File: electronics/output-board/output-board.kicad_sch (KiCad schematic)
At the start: 45 parts, among them J14 Arming switch, J17 Conn_01x02_Male, J19 Extra IO, J20 Ignition Detector, J3 12V In, J4 Conn_01x02, J5 SWD Header, J6 Conn_01x02, SW1 SW_Push_Dual, U1 MAX33012EASA+, U2 LD3985M33R_SOT23, U3 STM32F105VBH6, Y1 36MHz 9pF

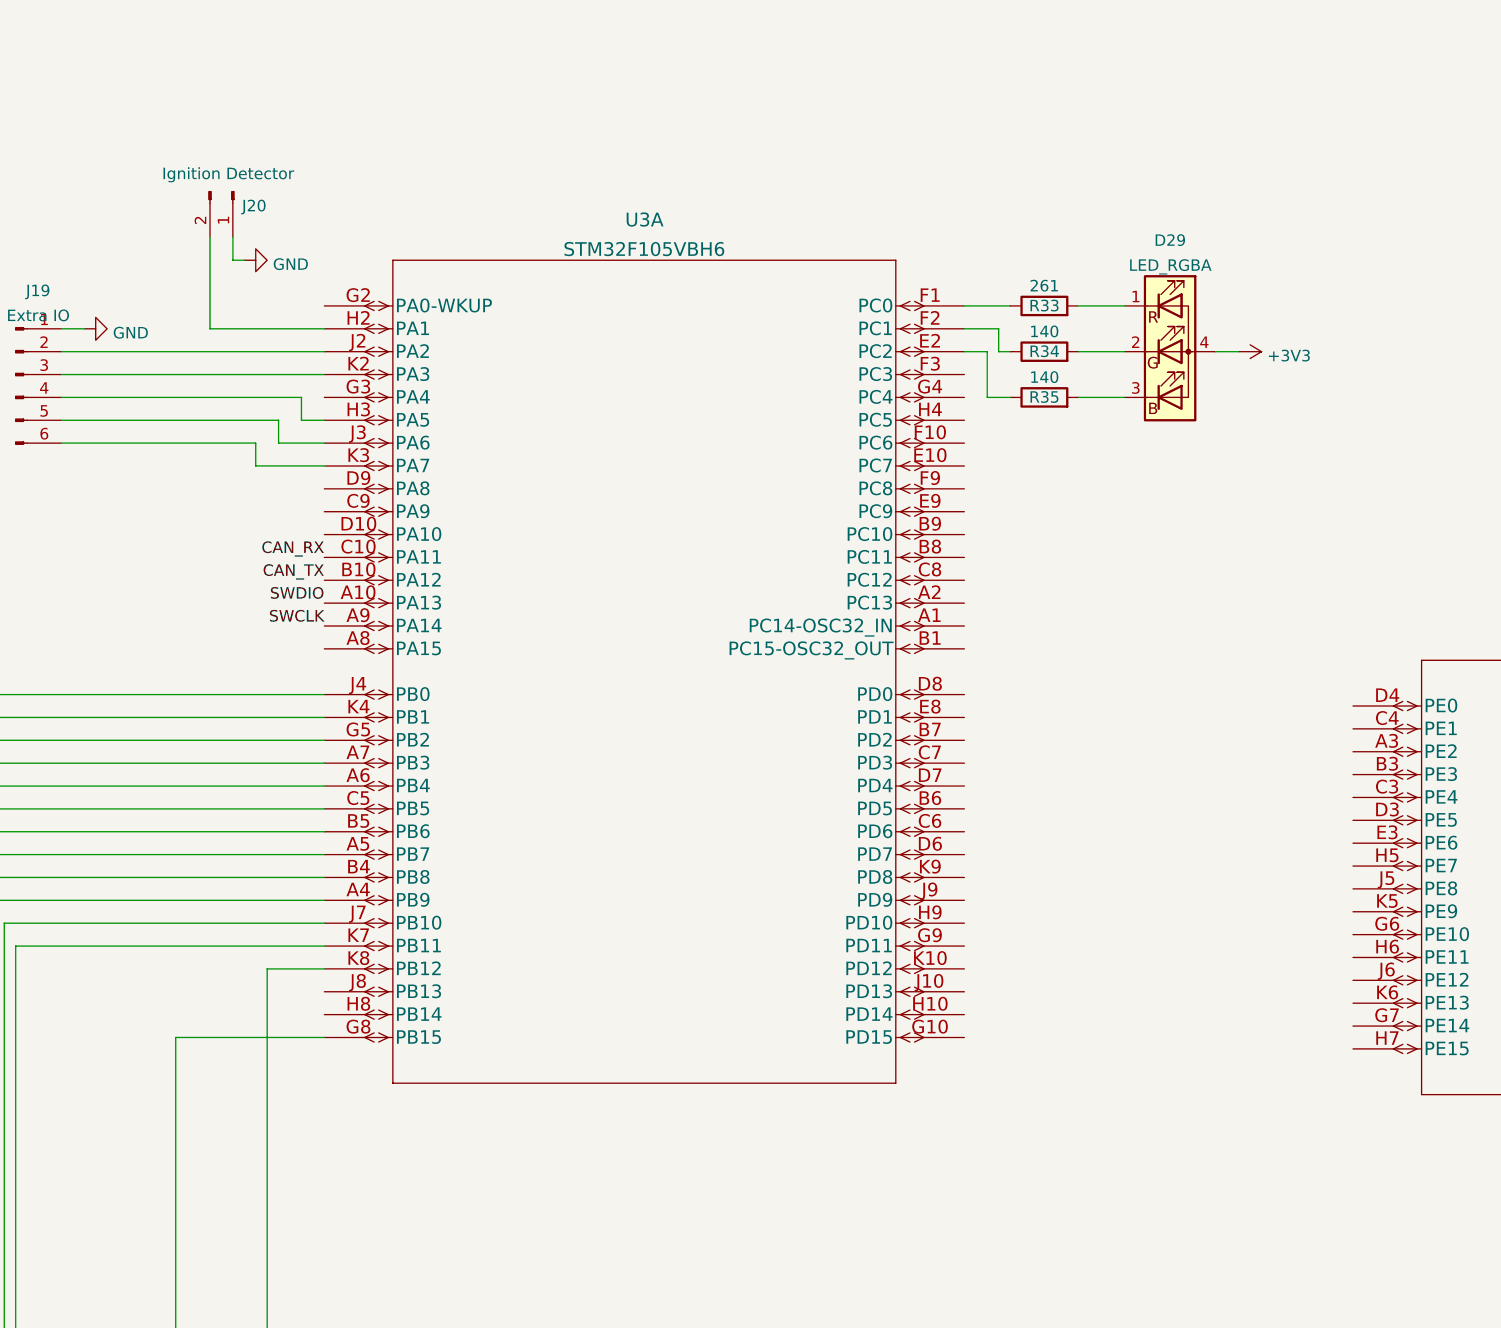
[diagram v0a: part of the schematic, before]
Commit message: Finishing touches on output board rev 2
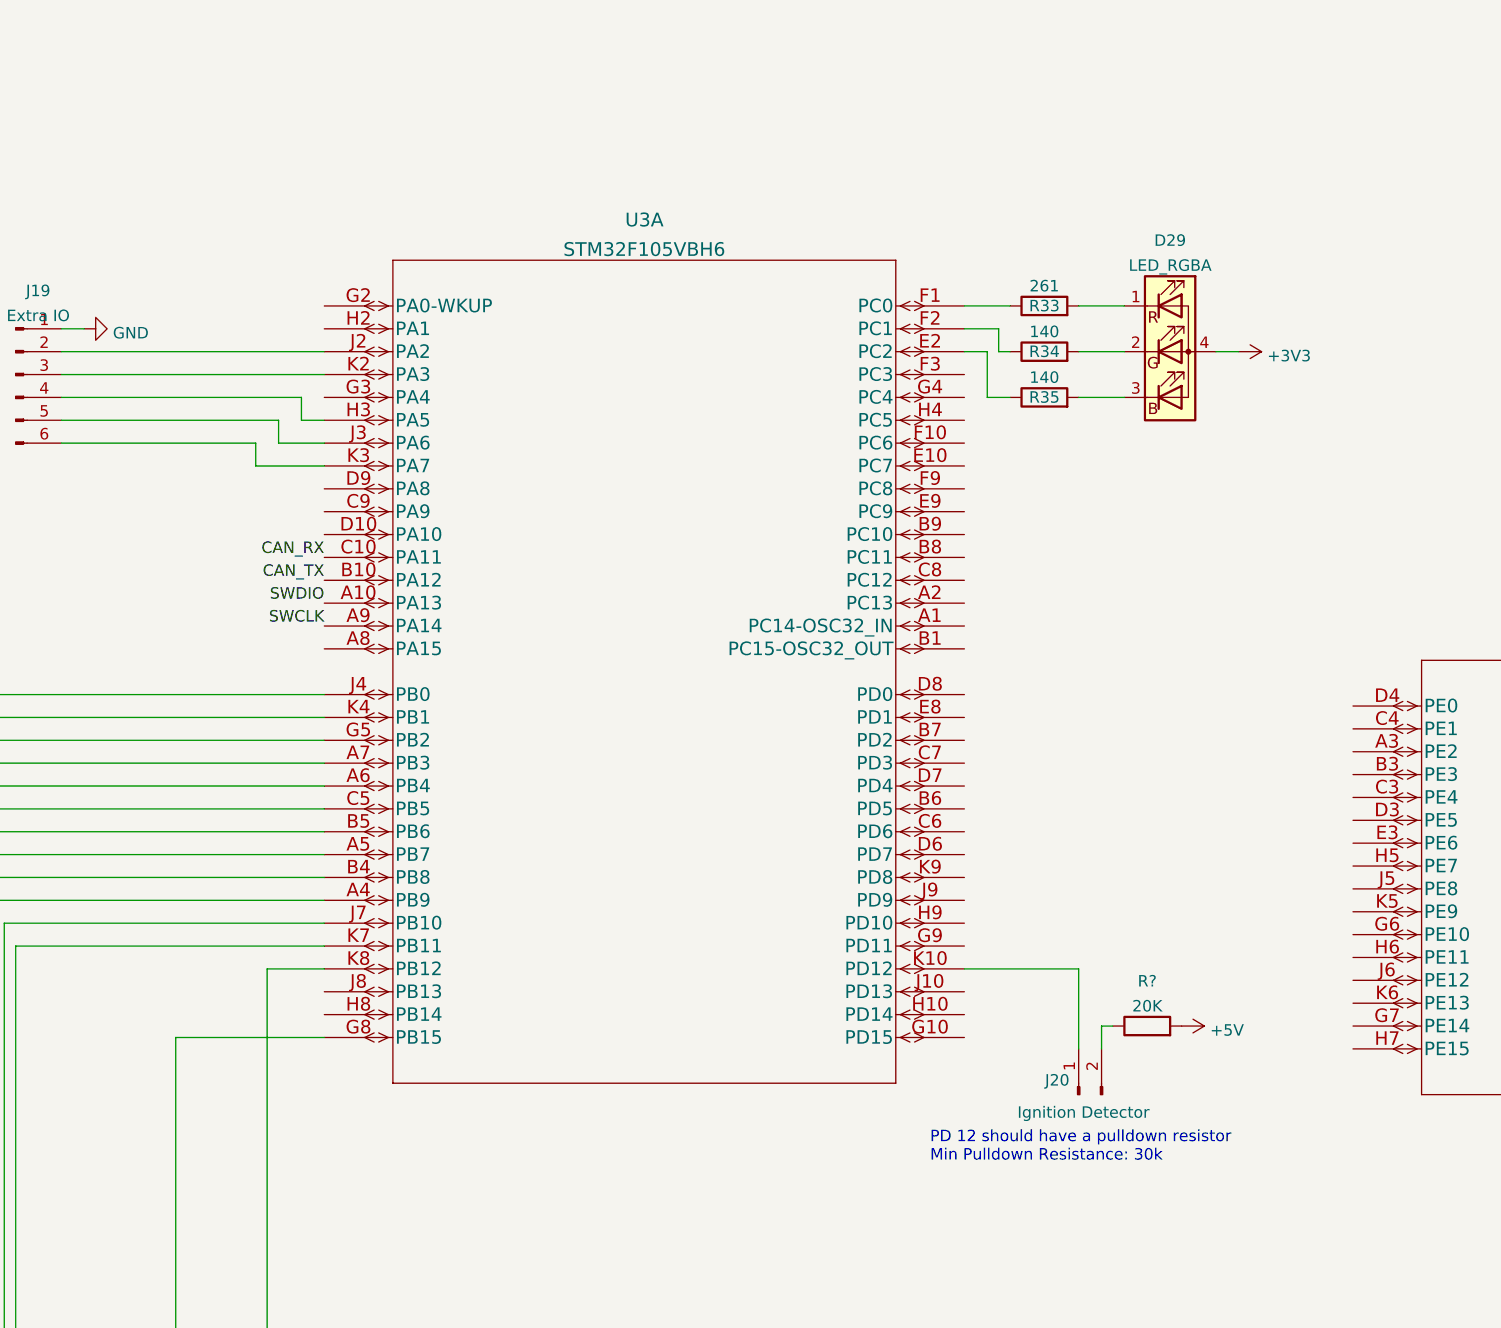
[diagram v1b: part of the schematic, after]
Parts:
- added R?: 20K, Resistor_SMD:R_0603_1608Metric, symbol Device:R
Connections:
- net +5V: now also R?.2
- net GND: no longer J20.1 (Pin_1)
- net at J20.2 (Pin_2): now also R?.1; no longer U3.H2 (PA1)
- net at U3.K10 (PD12): now also J20.1 (Pin_1)
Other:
- note added: "PD 12 should have a pulldown resistor Min Pulldown Resistance: 30k"
- moved on the sheet: J20
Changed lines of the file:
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@@
     (stroke (width 0) (type solid) (color 0 0 0 0))
+  )
+  (wire (pts (xy 251.46 148.59) (xy 252.73 148.59))
+    (stroke (width 0) (type default) (color 0 0 0 0))
   )
   (wire (pts (xy 238.76 78.74) (xy 238.76 73.66))
@@
     (stroke (width 0) (type default) (color 0 0 0 0))
   )
-  (wire (pts (xy 154.94 60.96) (xy 154.94 63.5))
-    (stroke (width 0) (type default) (color 0 0 0 0))
-  )
-  (wire (pts (xy 154.94 63.5) (xy 156.21 63.5))
-    (stroke (width 0) (type default) (color 0 0 0 0))
-  )
   (wire (pts (xy 284.48 204.47) (xy 285.75 204.47))
     (stroke (width 0) (type default) (color 0 0 0 0))
@@
     (stroke (width 0) (type default) (color 0 0 0 0))
   )
+  (wire (pts (xy 236.22 142.24) (xy 248.92 142.24))
+    (stroke (width 0) (type default) (color 0 0 0 0))
+  )
   (wire (pts (xy 332.74 194.31) (xy 332.74 186.69))
     (stroke (width 0) (type default) (color 0 0 0 0))
   )
+  (wire (pts (xy 251.46 151.13) (xy 251.46 148.59))
+    (stroke (width 0) (type default) (color 0 0 0 0))
+  )
   (wire (pts (xy 185.42 246.38) (xy 171.45 246.38))
     (stroke (width 0) (type default) (color 0 0 0 0))
@@
     (stroke (width 0) (type default) (color 0 0 0 0))
   )
+  (wire (pts (xy 248.92 151.13) (xy 248.92 142.24))
+    (stroke (width 0) (type default) (color 0 0 0 0))
+  )
   (wire (pts (xy 36.83 45.72) (xy 41.91 45.72))
     (stroke (width 0) (type solid) (color 0 0 0 0))
@@
   (wire (pts (xy 76.2 78.74) (xy 85.09 78.74))
     (stroke (width 0) (type solid) (color 0 0 0 0))
-  )
-  (wire (pts (xy 152.4 71.12) (xy 152.4 60.96))
-    (stroke (width 0) (type default) (color 0 0 0 0))
-  )
-  (wire (pts (xy 165.1 71.12) (xy 152.4 71.12))
-    (stroke (width 0) (type default) (color 0 0 0 0))
   )
   (wire (pts (xy 158.75 142.24) (xy 158.75 246.38))
@@
   (text "Hardcode to boot from flash memory" (at 367.03 115.57 180)
     (effects (font (size 0.5 0.5)) (justify right bottom))
+  )
+  (text "PD 12 should have a pulldown resistor\nMin Pulldown Resistance: 30k"
+    (at 232.41 163.83 0)
+    (effects (font (size 1.27 1.27)) (justify left bottom))
   )
   (label "CAN_RX" (at 165.1 96.52 180)
@@
     (pin "2")
   )
-  (symbol (lib_id "Connector:Conn_01x02_Male") (at 154.94 55.88 270) (unit 1)
-    (in_bom yes) (on_board yes)
-    (property "Reference" "J20" (id 0) (at 155.9561 57.4734 90)
-      (effects (font (size 1.27 1.27)) (justify left))
-    )
-    (property "Value" "Ignition Detector" (id 1) (at 147.0661 53.8985 90)
-      (effects (font (size 1.27 1.27)) (justify left))
-    )
-    (property "Footprint" "CustomFootprints:LatchingConnector2POS" (id 2) (at 154.94 55.88 0)
-      (effects (font (size 1.27 1.27)) hide)
-    )
-    (property "Datasheet" "~" (id 3) (at 154.94 55.88 0)
+  (symbol (lib_id "Device:R") (at 256.54 148.59 90) (unit 1)
+    (in_bom yes) (on_board yes) (fields_autoplaced)
+    (property "Reference" "R?" (id 0) (at 256.54 143.6075 90))
+    (property "Value" "20K" (id 1) (at 256.54 146.3826 90))
+    (property "Footprint" "Resistor_SMD:R_0603_1608Metric" (id 2) (at 256.54 150.368 90)
+      (effects (font (size 1.27 1.27)) hide)
+    )
+    (property "Datasheet" "~" (id 3) (at 256.54 148.59 0)
+      (effects (font (size 1.27 1.27)) hide)
+    )
+    (pin "1")
+    (pin "2")
+  )
+  (symbol (lib_id "Connector:Conn_01x02_Male") (at 248.92 156.21 90) (unit 1)
+    (in_bom yes) (on_board yes)
+    (property "Reference" "J20" (id 0) (at 247.9039 154.6166 90)
+      (effects (font (size 1.27 1.27)) (justify left))
+    )
+    (property "Value" "Ignition Detector" (id 1) (at 256.7939 158.1915 90)
+      (effects (font (size 1.27 1.27)) (justify left))
+    )
+    (property "Footprint" "CustomFootprints:LatchingConnector2POS" (id 2) (at 248.92 156.21 0)
+      (effects (font (size 1.27 1.27)) hide)
+    )
+    (property "Datasheet" "~" (id 3) (at 248.92 156.21 0)
       (effects (font (size 1.27 1.27)) hide)
     )
@@
     (pin "2")
   )
-  (symbol (lib_id "power:GND") (at 156.21 63.5 90) (unit 1)
-    (in_bom yes) (on_board yes) (fields_autoplaced)
-    (property "Reference" "#PWR0146" (id 0) (at 162.56 63.5 0)
-      (effects (font (size 1.27 1.27)) hide)
-    )
-    (property "Value" "GND" (id 1) (at 159.3851 63.979 90)
-      (effects (font (size 1.27 1.27)) (justify right))
-    )
-    (property "Footprint" "" (id 2) (at 156.21 63.5 0)
-      (effects (font (size 1.27 1.27)) hide)
-    )
-    (property "Datasheet" "" (id 3) (at 156.21 63.5 0)
-      (effects (font (size 1.27 1.27)) hide)
-    )
-    (pin "1")
-  )
   (symbol (lib_id "power:GND") (at 355.6 214.63 90) (unit 1)
     (in_bom yes) (on_board yes) (fields_autoplaced)
@@
     )
     (property "Datasheet" "" (id 3) (at 355.6 214.63 0)
+      (effects (font (size 1.27 1.27)) hide)
+    )
+    (pin "1")
+  )
+  (symbol (lib_id "power:+5V") (at 260.35 148.59 270) (unit 1)
+    (in_bom yes) (on_board yes) (fields_autoplaced)
+    (property "Reference" "#PWR?" (id 0) (at 256.54 148.59 0)
+      (effects (font (size 1.27 1.27)) hide)
+    )
+    (property "Value" "+5V" (id 1) (at 263.525 149.069 90)
+      (effects (font (size 1.27 1.27)) (justify left))
+    )
+    (property "Footprint" "" (id 2) (at 260.35 148.59 0)
+      (effects (font (size 1.27 1.27)) hide)
+    )
+    (property "Datasheet" "" (id 3) (at 260.35 148.59 0)
       (effects (font (size 1.27 1.27)) hide)
     )
@@
       (reference "#PWR0145") (unit 1) (value "GND") (footprint "")
     )
-    (path "/fd3f52cc-6c59-4511-9709-ca40718f93e3"
-      (reference "#PWR0146") (unit 1) (value "GND") (footprint "")
-    )
     (path "/3b97f976-e2c2-46d6-92c9-63c2a4bf9ffe"
       (reference "#PWR0147") (unit 1) (value "GND") (footprint "")
@@
       (reference "#PWR0150") (unit 1) (value "+3V3") (footprint "")
     )
+    (path "/fdc7cf50-f28c-4ff5-9959-b2576c8c86f0"
+      (reference "#PWR?") (unit 1) (value "+5V") (footprint "")
+    )
     (path "/2c82cb5d-5242-4074-b9d4-e6795eb314a0"
       (reference "C1") (unit 1) (value "1uF") (footprint "Capacitor_SMD:C_0603_1608Metric")
@@
       (reference "R35") (unit 1) (value "140") (footprint "Resistor_SMD:R_0603_1608Metric")
     )
+    (path "/e65af263-eac2-4cbe-a5b8-9f479ef7f0b7"
+      (reference "R?") (unit 1) (value "20K") (footprint "Resistor_SMD:R_0603_1608Metric")
+    )
     (path "/5a984209-2501-4b3c-984e-c60f26a02fd0"

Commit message: changed can transciever
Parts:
- removed U1: MAX33012EASA+, MAX33012EASA+:MAX33012EASA+, symbol MAX33012EASA+:MAX33012EASA+
- added C14: 100nF, Capacitor_SMD:C_0603_1608Metric, symbol Device:C_Small
- added R36: 120, Resistor_SMD:R_0603_1608Metric, symbol Device:R
- added U1: MAX33014EATB+, MAX33014E:MAX33014EATB&plus_, symbol 2022-03-14_22-38-09:MAX33014EATB+
- gave numbers to parts that had none: 1
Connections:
- net +3V3: now also U1.7 (VL)
- net +5V: now also C14.1, U1.4 (VDD)
- net CAN_RX: now also U1.5 (RXD)
- net CAN_TX: now also U1.1 (TXD)
- net GND: now also C14.2, U1.10 (STBY), U1.2 (LPBK), U1.3 (GND)
- net at J6.2 (Pin_2): now also R36.1, U1.8 (CANL)
- net at J6.1 (Pin_1): now also R36.2, U1.9 (CANH)
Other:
- moved on the sheet: J6
